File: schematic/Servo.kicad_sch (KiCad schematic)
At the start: 0 parts

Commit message: Create servo header schematic
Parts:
- added J5: Servo, symbol Connector:Conn_01x03_Pin
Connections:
- new net +5V: J5.2 (Pin_2)
- new net GND: J5.3 (Pin_3)
- new net SERVO: J5.1 (Pin_1)
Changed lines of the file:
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@@
     (rev "v1")
   )
+  (wire (pts (xy 139.7 99.06) (xy 139.7 101.6))
+    (stroke (width 0) (type default))
+  )
+  (wire (pts (xy 147.32 104.14) (xy 152.4 104.14))
+    (stroke (width 0) (type default))
+  )
+  (wire (pts (xy 149.86 99.06) (xy 152.4 99.06))
+    (stroke (width 0) (type default))
+  )
+  (wire (pts (xy 139.7 101.6) (xy 152.4 101.6))
+    (stroke (width 0) (type default))
+  )
+  (wire (pts (xy 147.32 106.68) (xy 147.32 104.14))
+    (stroke (width 0) (type default))
+  )
+  (hierarchical_label "SERVO" (shape input) (at 149.86 99.06 180) (fields_autoplaced)
+    (effects (font (size 1.27 1.27)) (justify right))
+  )
+  (symbol (lib_id "power:+5V") (at 139.7 99.06 0) (unit 1)
+    (in_bom yes) (on_board yes) (dnp no) (fields_autoplaced)
+    (property "Reference" "#PWR036" (at 139.7 102.87 0)
+      (effects (font (size 1.27 1.27)) hide)
+    )
+    (property "Value" "+5V" (at 139.7 95.25 0)
+      (effects (font (size 1.27 1.27)))
+    )
+    (property "Footprint" "" (at 139.7 99.06 0)
+      (effects (font (size 1.27 1.27)) hide)
+    )
+    (property "Datasheet" "" (at 139.7 99.06 0)
+      (effects (font (size 1.27 1.27)) hide)
+    )
+    (pin "1")
+    (instances
+      (project "ISSptr"
+        (path "/c978750c-b285-44b2-8d41-37a456977bcd/6312e27f-09b4-4a8c-98e1-124dfb1b8b7c"
+          (reference "#PWR036") (unit 1)
+        )
+      )
+    )
+  )
+  (symbol (lib_id "power:GND") (at 147.32 106.68 0) (unit 1)
+    (in_bom yes) (on_board yes) (dnp no) (fields_autoplaced)
+    (property "Reference" "#PWR037" (at 147.32 113.03 0)
+      (effects (font (size 1.27 1.27)) hide)
+    )
+    (property "Value" "GND" (at 147.32 111.76 0)
+      (effects (font (size 1.27 1.27)))
+    )
+    (property "Footprint" "" (at 147.32 106.68 0)
+      (effects (font (size 1.27 1.27)) hide)
+    )
+    (property "Datasheet" "" (at 147.32 106.68 0)
+      (effects (font (size 1.27 1.27)) hide)
+    )
+    (pin "1")
+    (instances
+      (project "ISSptr"
+        (path "/c978750c-b285-44b2-8d41-37a456977bcd/6312e27f-09b4-4a8c-98e1-124dfb1b8b7c"
+          (reference "#PWR037") (unit 1)
+        )
+      )
+    )
+  )
+  (symbol (lib_id "Connector:Conn_01x03_Pin") (at 157.48 101.6 0) (mirror y) (unit 1)
+    (in_bom yes) (on_board yes) (dnp no)
+    (property "Reference" "J5" (at 160.02 100.33 0)
+      (effects (font (size 1.27 1.27)) (justify right))
+    )
+    (property "Value" "Servo" (at 160.02 102.87 0)
+      (effects (font (size 1.27 1.27)) (justify right))
+    )
+    (property "Footprint" "" (at 157.48 101.6 0)
+      (effects (font (size 1.27 1.27)) hide)
+    )
+    (property "Datasheet" "~" (at 157.48 101.6 0)
+      (effects (font (size 1.27 1.27)) hide)
+    )
+    (pin "1")
+    (pin "2")
+    (pin "3")
+    (instances
+      (project "ISSptr"
+        (path "/c978750c-b285-44b2-8d41-37a456977bcd/6312e27f-09b4-4a8c-98e1-124dfb1b8b7c"
+          (reference "J5") (unit 1)
+        )
+      )
+    )
+  )
 )

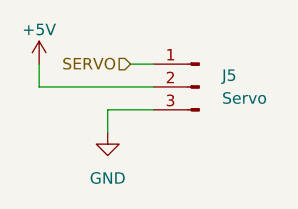
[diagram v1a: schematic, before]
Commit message: Assign footprints
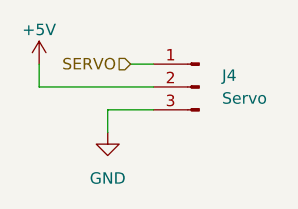
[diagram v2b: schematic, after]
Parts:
- J4: renamed from J5; footprint (none) -> Connector_PinHeader_2.54mm:PinHeader_1x03_P2.54mm_Horizontal
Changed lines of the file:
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@@
   (symbol (lib_id "Connector:Conn_01x03_Pin") (at 157.48 101.6 0) (mirror y) (unit 1)
     (in_bom yes) (on_board yes) (dnp no)
-    (property "Reference" "J5" (at 160.02 100.33 0)
+    (property "Reference" "J4" (at 160.02 100.33 0)
       (effects (font (size 1.27 1.27)) (justify right))
     )
@@
       (effects (font (size 1.27 1.27)) (justify right))
     )
-    (property "Footprint" "" (at 157.48 101.6 0)
+    (property "Footprint" "Connector_PinHeader_2.54mm:PinHeader_1x03_P2.54mm_Horizontal" (at 157.48 101.6 0)
       (effects (font (size 1.27 1.27)) hide)
     )
@@
       (project "ISSptr"
         (path "/c978750c-b285-44b2-8d41-37a456977bcd/6312e27f-09b4-4a8c-98e1-124dfb1b8b7c"
-          (reference "J5") (unit 1)
+          (reference "J4") (unit 1)
         )
       )
